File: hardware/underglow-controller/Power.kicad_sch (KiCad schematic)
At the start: 17 parts, among them Q7 Q_PMOS_GDS, U8 ADP2303ARDZ-3.3

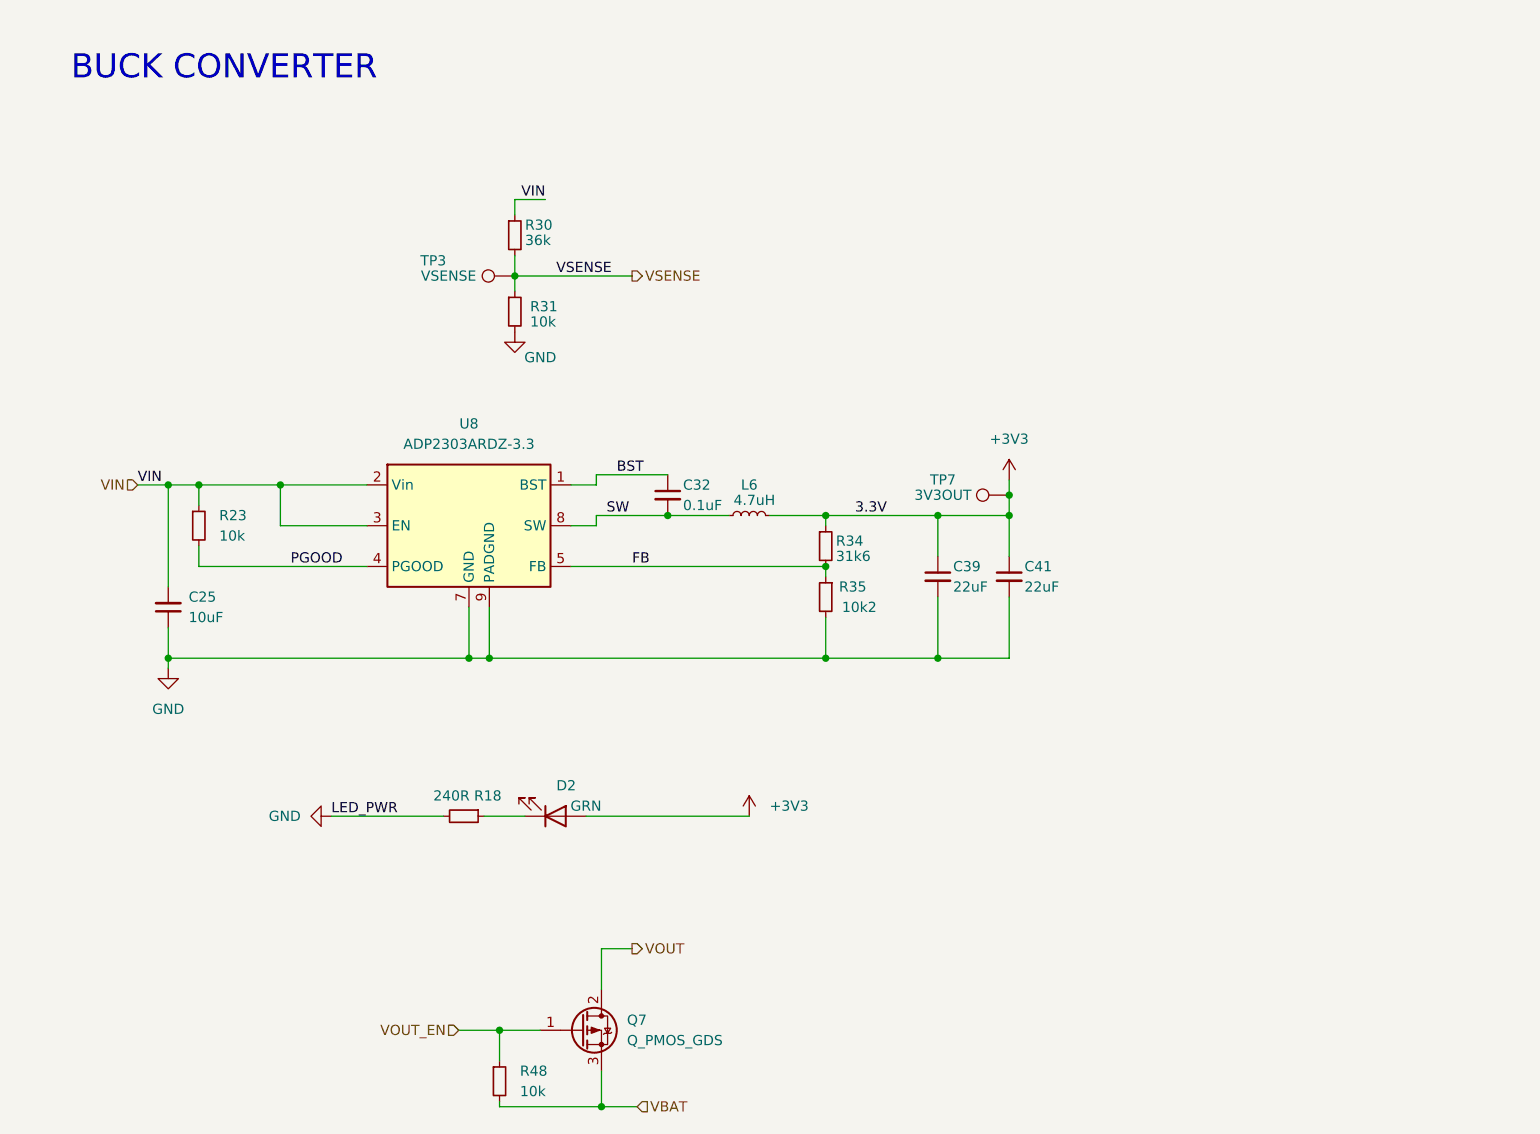
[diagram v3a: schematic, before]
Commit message: add USB VIN
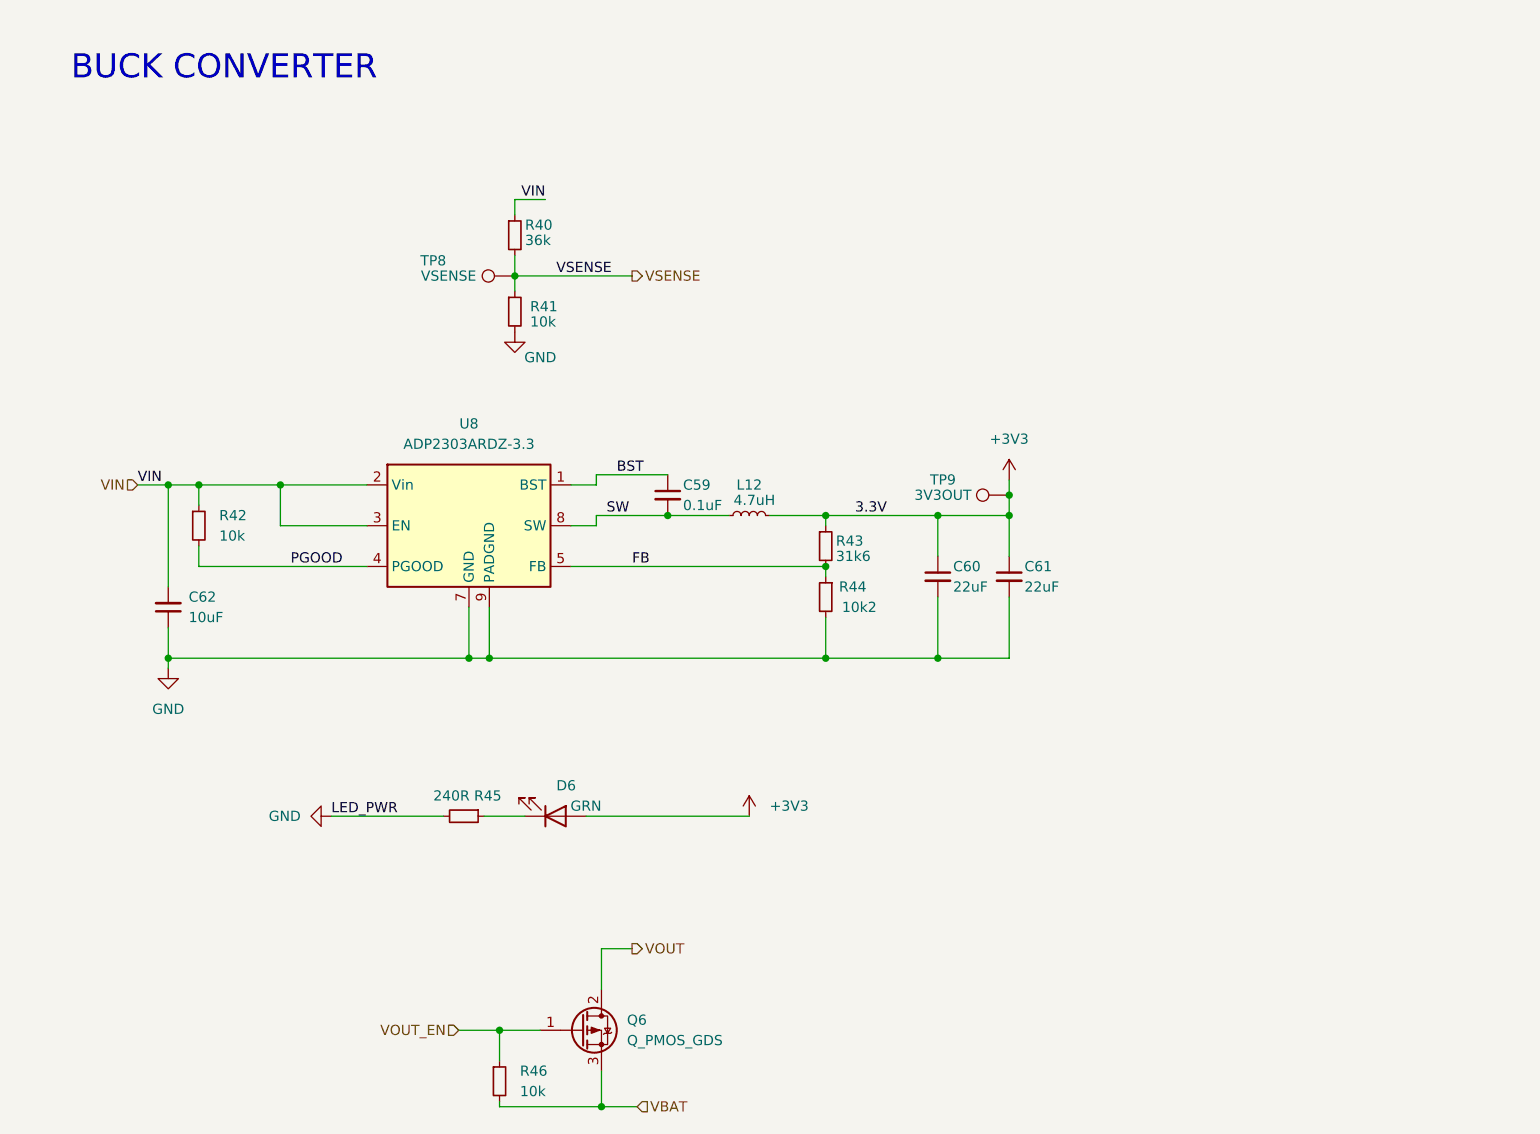
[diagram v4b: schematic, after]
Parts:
- U8: footprint Package_SO:SOIC-8-1EP_3.9x4.9mm_P1.27mm_EP2.29x3mm -> Package_SO:SOIC-8-1EP_3.9x4.9mm_P1.27mm_EP2.29x3mm_ThermalVias
- renumbered C32 to C59, C39 to C60, C41 to C61, C25 to C62, D2 to D6, L6 to L12, Q7 to Q6, R30 to R40, R31 to R41, R23 to R42, R34 to R43, R35 to R44, R18 to R45, R48 to R46, TP3 to TP8, TP7 to TP9
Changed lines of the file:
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@@
   (symbol (lib_id "Device:R_Small") (at 33.02 76.2 0) (unit 1)
     (in_bom yes) (on_board yes) (fields_autoplaced)
-    (property "Reference" "R23" (id 0) (at 35.56 74.9299 0)
+    (property "Reference" "R42" (id 0) (at 35.56 74.9299 0)
       (effects (font (size 1.27 1.27)) (justify left))
     )
@@
   (symbol (lib_id "Device:R_Small") (at 111.125 85.09 0) (mirror y) (unit 1)
     (in_bom yes) (on_board yes)
-    (property "Reference" "R35" (id 0) (at 116.205 83.82 0)
+    (property "Reference" "R44" (id 0) (at 116.205 83.82 0)
       (effects (font (size 1.27 1.27)) (justify left))
     )
@@
   (symbol (lib_id "Device:C_Small") (at 133.985 82.55 0) (unit 1)
     (in_bom yes) (on_board yes)
-    (property "Reference" "C41" (id 0) (at 135.89 81.2862 0)
+    (property "Reference" "C61" (id 0) (at 135.89 81.2862 0)
       (effects (font (size 1.27 1.27)) (justify left))
     )
@@
   (symbol (lib_id "power:GND") (at 49.53 112.395 270) (unit 1)
     (in_bom yes) (on_board yes) (fields_autoplaced)
-    (property "Reference" "#PWR0127" (id 0) (at 43.18 112.395 0)
+    (property "Reference" "#PWR085" (id 0) (at 43.18 112.395 0)
       (effects (font (size 1.27 1.27)) hide)
     )
@@
   (symbol (lib_id "Device:R_Small") (at 72.39 40.005 0) (unit 1)
     (in_bom yes) (on_board yes)
-    (property "Reference" "R30" (id 0) (at 73.66 38.735 0)
+    (property "Reference" "R40" (id 0) (at 73.66 38.735 0)
       (effects (font (size 1.27 1.27)) (justify left))
     )
@@
   (symbol (lib_id "Device:C_Small") (at 125.095 82.55 0) (unit 1)
     (in_bom yes) (on_board yes)
-    (property "Reference" "C39" (id 0) (at 127 81.2862 0)
+    (property "Reference" "C60" (id 0) (at 127 81.2862 0)
       (effects (font (size 1.27 1.27)) (justify left))
     )
@@
   (symbol (lib_id "Device:C_Small") (at 29.21 86.36 180) (unit 1)
     (in_bom yes) (on_board yes)
-    (property "Reference" "C25" (id 0) (at 31.75 85.0835 0)
+    (property "Reference" "C62" (id 0) (at 31.75 85.0835 0)
       (effects (font (size 1.27 1.27)) (justify right))
     )
@@
     (property "Reference" "U8" (id 0) (at 66.675 63.5 0))
     (property "Value" "ADP2303ARDZ-3.3" (id 1) (at 66.675 66.04 0))
-    (property "Footprint" "Package_SO:SOIC-8-1EP_3.9x4.9mm_P1.27mm_EP2.29x3mm" (id 2) (at 70.485 85.09 0)
+    (property "Footprint" "Package_SO:SOIC-8-1EP_3.9x4.9mm_P1.27mm_EP2.29x3mm_ThermalVias" (id 2) (at 70.485 85.09 0)
       (effects (font (size 1.27 1.27)) (justify left) hide)
     )
@@
   (symbol (lib_id "Connector:TestPoint") (at 133.985 72.39 90) (unit 1)
     (in_bom yes) (on_board yes)
-    (property "Reference" "TP7" (id 0) (at 125.73 70.485 90))
+    (property "Reference" "TP9" (id 0) (at 125.73 70.485 90))
     (property "Value" "3V3OUT" (id 1) (at 125.73 72.39 90))
     (property "Footprint" "TestPoint:TestPoint_Pad_D1.0mm" (id 2) (at 133.985 67.31 0)
@@
   (symbol (lib_id "Device:L_Small") (at 101.6 74.93 90) (unit 1)
     (in_bom yes) (on_board yes)
-    (property "Reference" "L6" (id 0) (at 101.6 71.12 90))
+    (property "Reference" "L12" (id 0) (at 101.6 71.12 90))
     (property "Value" "4.7uH" (id 1) (at 102.235 73.025 90))
     (property "Footprint" "Inductor_SMD:L_Bourns-SRN6028" (id 2) (at 101.6 74.93 0)
@@
   (symbol (lib_id "Device:R_Small") (at 111.125 78.74 0) (unit 1)
     (in_bom yes) (on_board yes)
-    (property "Reference" "R34" (id 0) (at 112.395 78.1049 0)
+    (property "Reference" "R43" (id 0) (at 112.395 78.1049 0)
       (effects (font (size 1.27 1.27)) (justify left))
     )
@@
   (symbol (lib_id "Device:C_Small") (at 91.44 72.39 0) (unit 1)
     (in_bom yes) (on_board yes)
-    (property "Reference" "C32" (id 0) (at 93.345 71.1262 0)
+    (property "Reference" "C59" (id 0) (at 93.345 71.1262 0)
       (effects (font (size 1.27 1.27)) (justify left))
     )
@@
   (symbol (lib_id "Device:LED") (at 77.47 112.395 0) (mirror x) (unit 1)
     (in_bom yes) (on_board yes)
-    (property "Reference" "D2" (id 0) (at 80.01 108.585 0)
+    (property "Reference" "D6" (id 0) (at 80.01 108.585 0)
       (effects (font (size 1.27 1.27)) (justify right))
     )
@@
   (symbol (lib_id "Device:R_Small") (at 66.04 112.395 270) (unit 1)
     (in_bom yes) (on_board yes)
-    (property "Reference" "R18" (id 0) (at 67.31 109.855 90)
+    (property "Reference" "R45" (id 0) (at 67.31 109.855 90)
       (effects (font (size 1.27 1.27)) (justify left))
     )
@@
   (symbol (lib_id "Device:R_Small") (at 72.39 49.53 0) (unit 1)
     (in_bom yes) (on_board yes)
-    (property "Reference" "R31" (id 0) (at 74.295 48.895 0)
+    (property "Reference" "R41" (id 0) (at 74.295 48.895 0)
       (effects (font (size 1.27 1.27)) (justify left))
     )
@@
   (symbol (lib_id "Device:Q_PMOS_GDS") (at 80.645 139.065 0) (unit 1)
     (in_bom yes) (on_board yes) (fields_autoplaced)
-    (property "Reference" "Q7" (id 0) (at 86.36 137.7949 0)
+    (property "Reference" "Q6" (id 0) (at 86.36 137.7949 0)
       (effects (font (size 1.27 1.27)) (justify left))
     )
@@
   (symbol (lib_id "Device:R_Small") (at 70.485 145.415 0) (unit 1)
     (in_bom yes) (on_board yes) (fields_autoplaced)
-    (property "Reference" "R48" (id 0) (at 73.025 144.1449 0)
+    (property "Reference" "R46" (id 0) (at 73.025 144.1449 0)
       (effects (font (size 1.27 1.27)) (justify left))
     )
@@
   (symbol (lib_id "power:GND") (at 72.39 52.07 0) (unit 1)
     (in_bom yes) (on_board yes)
-    (property "Reference" "#PWR050" (id 0) (at 72.39 58.42 0)
+    (property "Reference" "#PWR082" (id 0) (at 72.39 58.42 0)
       (effects (font (size 1.27 1.27)) hide)
     )
@@
   (symbol (lib_id "power:+3V3") (at 101.6 112.395 0) (unit 1)
     (in_bom yes) (on_board yes) (fields_autoplaced)
-    (property "Reference" "#PWR034" (id 0) (at 101.6 116.205 0)
+    (property "Reference" "#PWR086" (id 0) (at 101.6 116.205 0)
       (effects (font (size 1.27 1.27)) hide)
     )
@@
   (symbol (lib_id "power:GND") (at 29.21 93.98 0) (unit 1)
     (in_bom yes) (on_board yes) (fields_autoplaced)
-    (property "Reference" "#PWR042" (id 0) (at 29.21 100.33 0)
+    (property "Reference" "#PWR084" (id 0) (at 29.21 100.33 0)
       (effects (font (size 1.27 1.27)) hide)
     )
@@
   (symbol (lib_id "power:+3V3") (at 133.985 70.485 0) (unit 1)
     (in_bom yes) (on_board yes) (fields_autoplaced)
-    (property "Reference" "#PWR058" (id 0) (at 133.985 74.295 0)
+    (property "Reference" "#PWR083" (id 0) (at 133.985 74.295 0)
       (effects (font (size 1.27 1.27)) hide)
     )
@@
   (symbol (lib_id "Connector:TestPoint") (at 72.39 45.085 90) (unit 1)
     (in_bom yes) (on_board yes)
-    (property "Reference" "TP3" (id 0) (at 62.23 43.18 90))
+    (property "Reference" "TP8" (id 0) (at 62.23 43.18 90))
     (property "Value" "VSENSE" (id 1) (at 64.135 45.085 90))
     (property "Footprint" "TestPoint:TestPoint_Pad_D1.0mm" (id 2) (at 72.39 40.005 0)

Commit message: Hardware updates
* fix messed up +12v pin
* add a ground output for neopixels on both channels
* add a i2c microphone
* clean up schematic
* calculate component values for the LED drivers
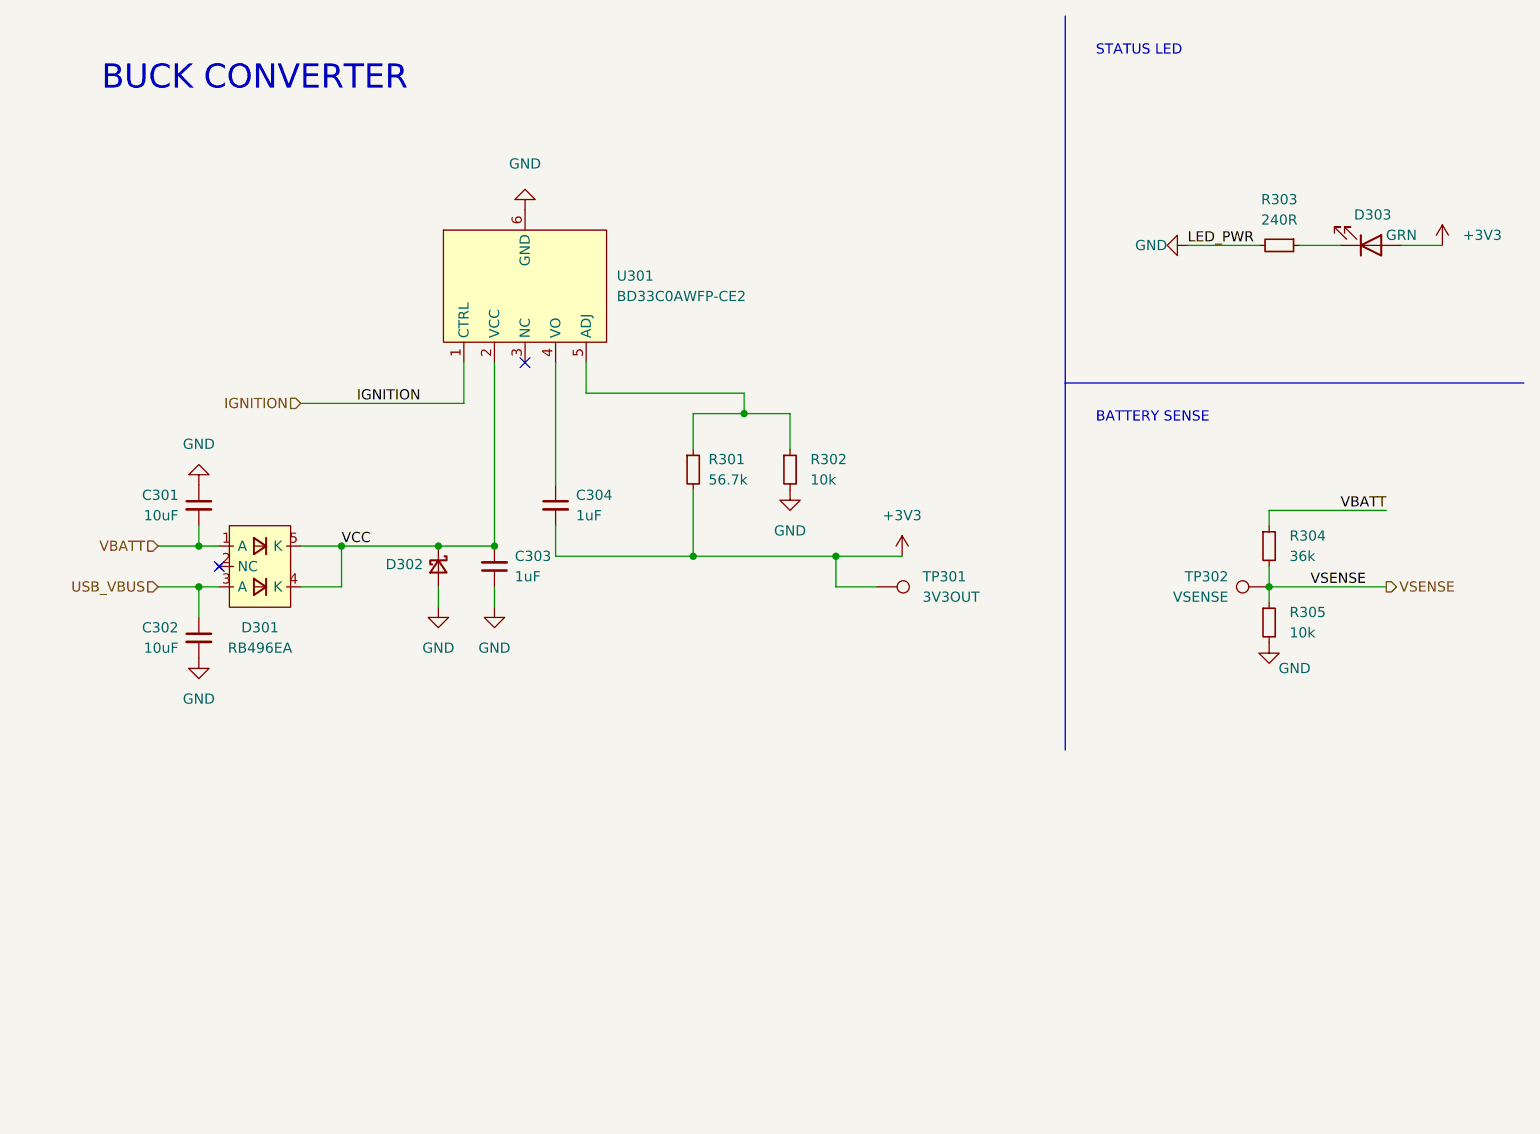
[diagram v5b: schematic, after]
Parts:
- removed C59: 0.1uF, Capacitor_SMD:C_0805_2012Metric, symbol Device:C_Small
- removed C60, C61: 22uF, Capacitor_SMD:C_0805_2012Metric, symbol Device:C_Small
- removed L12: 4.7uH, Inductor_SMD:L_Bourns-SRN6028, symbol Device:L_Small
- removed Q6: Q_PMOS_GDS, Package_TO_SOT_SMD:TO-252-2, symbol Device:Q_PMOS_GDS
- removed R42, R46: 10k, Resistor_SMD:R_0603_1608Metric, symbol Device:R_Small
- removed R43: 31k6, Resistor_SMD:R_0603_1608Metric, symbol Device:R_Small
- removed R44: 10k2, Resistor_SMD:R_0603_1608Metric, symbol Device:R_Small
- removed U8: ADP2303ARDZ-3.3, Package_SO:SOIC-8-1EP_3.9x4.9mm_P1.27mm_EP2.29x3mm_ThermalVias, symbol Regulator_Switching:ADP2303ARDZ-3.3
- added C301, C302: 10uF, Capacitor_SMD:C_0805_2012Metric, symbol Device:C_Small
- added C304: 1uF, Capacitor_SMD:C_0805_2012Metric, symbol Device:C_Small
- added D301: RB496EA, Package_TO_SOT_SMD:SOT-23-5, symbol ConeCodes:RB496EA
- added D302: D_Schottky_Small, Diode_SMD:D_SMA, symbol Device:D_Schottky_Small
- added R301: 56.7k, Resistor_SMD:R_0805_2012Metric, symbol Device:R_Small
- added R302: 10k, Resistor_SMD:R_0805_2012Metric, symbol Device:R_Small
- added U301: BD33C0AWFP-CE2, Package_TO_SOT_SMD:TO-252-5_TabPin6, symbol ConeCodes:BD33C0AWFP-CE2
- C303: renamed from C62; value 10uF -> 1uF; MPN CL21A106KAFN3NE -> (none)
- renumbered D6 to D303, R45 to R303, R40 to R304, R41 to R305, TP9 to TP301, TP8 to TP302
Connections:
- net +3V3: now also C304.2, R301.2
- net GND: now also C301.1, C302.2, D302.2 (A), R302.2, U301.6 (GND)
- net VIN renamed VBATT
- net VBATT: now also C301.2, D301.1 (A); no longer C303.2
- new net: R301.1, R302.1, U301.5 (ADJ)
- new net: C304.1, U301.4 (VO)
- new net IGNITION: U301.1 (CTRL)
- new net USB_VBUS: C302.1, D301.3 (A)
- new net VCC: C303.2, D301.4 (K), D301.5 (K), D302.1 (K), U301.2 (VCC)
- no-connect marks 0 -> 2
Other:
- note added: "BATTERY SENSE"
- note added: "STATUS LED"
- title: CAN RGB Controller -> CAN RGB Controller V5
- moved on the sheet: C303, D303, R303, R304, R305, TP301, TP302

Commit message: Bom fillout + wiring
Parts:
- R301: MPN (none) -> RMCF0805FT57K6
- R302: MPN (none) -> RNCP0805FTD10K0
- U301: MPN (none) -> BD33C0AWFP-CE2
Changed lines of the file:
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@@
+      (effects (font (size 1.27 1.27)) hide)
+    )
+    (property "Description" "RES 57.6K OHM 1% 1/8W 0805" (id 4) (at 94.615 69.215 0)
+      (effects (font (size 1.27 1.27)) hide)
+    )
+    (property "MPN" "RMCF0805FT57K6" (id 5) (at 94.615 69.215 0)
       (effects (font (size 1.27 1.27)) hide)
     )
@@
     )
     (property "Datasheet" "" (id 3) (at 85.09 52.07 0)
+      (effects (font (size 1.27 1.27)) hide)
+    )
+    (property "MPN" "BD33C0AWFP-CE2" (id 4) (at 73.66 48.26 0)
       (effects (font (size 1.27 1.27)) hide)
     )
@@
       (effects (font (size 1.27 1.27)) hide)
     )
+    (property "Description" "RES 10K OHM 1% 1/4W 0805" (id 4) (at 106.68 69.215 0)
+      (effects (font (size 1.27 1.27)) hide)
+    )
+    (property "MPN" "RNCP0805FTD10K0" (id 5) (at 106.68 69.215 0)
+      (effects (font (size 1.27 1.27)) hide)
+    )

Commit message: hw updates based on prototype issues
* Removes unused hardware and firmware projectes
* Adds some documentation and bom
* cleanup READMEs
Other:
- company: cone.codes -> Connor Rigby
- title: CAN RGB Controller V5 -> ${Title}
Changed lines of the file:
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@@
   (paper "A5")
   (title_block
-    (title "CAN RGB Controller V5")
+    (title "${Title}")
     (date "2022-06-24")
-    (rev "A")
-    (company "cone.codes")
+    (rev "${Revision}")
+    (company "Connor Rigby")
     (comment 1 "https://github.com/miata-bot/can-link")
+    (comment 2 "https://cone.codes")
   )
   (junction (at 112.395 80.01) (diameter 0) (color 0 0 0 0)
